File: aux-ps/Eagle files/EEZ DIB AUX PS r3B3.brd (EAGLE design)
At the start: 230.5 x 60 mm, 82 parts, among them IC1 BD00FC0WFP-E2, IC2 MAX31760AEE+, J1 PF0030/PC, J2 1-726388-2, J3 1-726388-2, J4 SWEB 8094 AU/GN, Q1 BTA26-600, Q2 BTA26-600, Q3 2N7002, Q4 2N7002, Q5 2N7002, SW1 DF62J12S2AHQA, SW2 EVQP7A01P, X1 39-28-1063, X2 39-30-1039, X3 DS1013-16SSIB1, X4 47053-1000, X5 N.C.

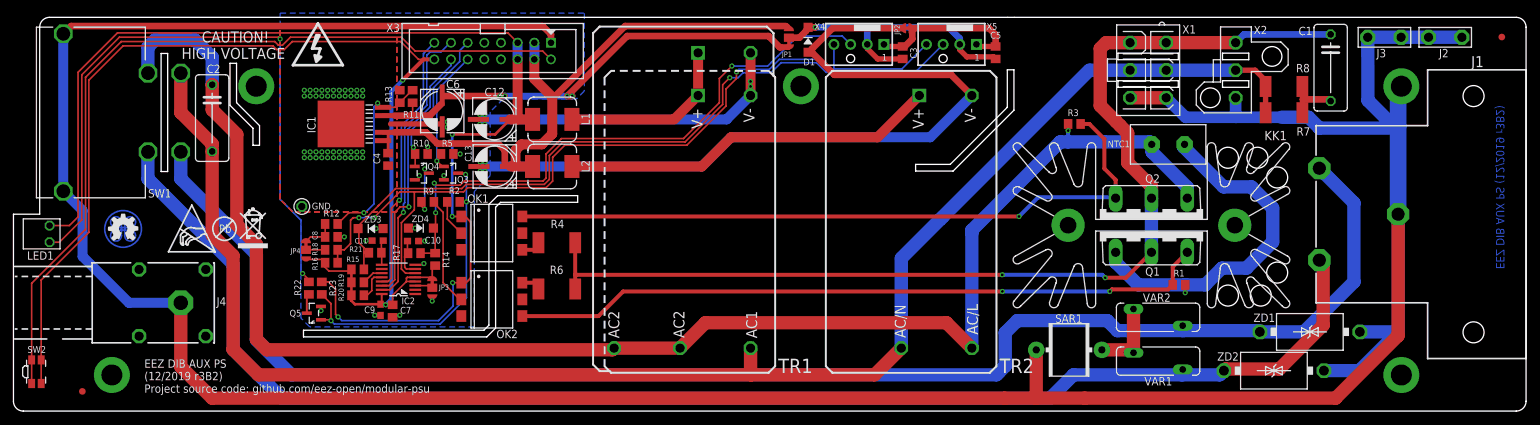
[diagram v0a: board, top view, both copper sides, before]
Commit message: #63, remove BOOT sw from AUX-PS
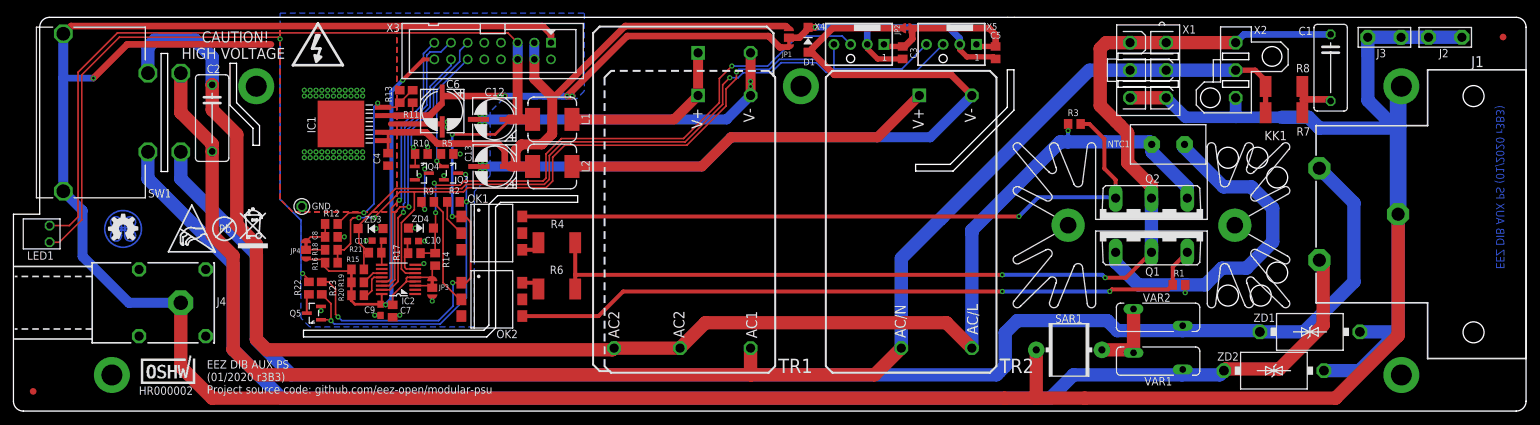
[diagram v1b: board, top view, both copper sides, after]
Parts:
- removed SW2: EVQP7A01P, EEZ_switches:PANASONIC_EVQP
- added OSHWA: HR000002, EEZ_Lib1:CERT-SMALL-SILK
- SW1: value DF62J12S2AHQA -> 1552.2602
- moved FM1 7.50 mm to (3.00, 3.00)
- moved FM2 0.20 mm to (227.0, 57.0)
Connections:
- net +3V3: no longer SW2.2.1, SW2.2.2
- net MBOOT: no longer SW2.1.1, SW2.1.2
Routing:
- net MBOOT: track 125.4 -> 0.00 mm
- net +3V3: track 182.6 -> 76.7 mm
- net PE: track 490.2 -> 524.0 mm, vias 2 -> 3
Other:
- board text added: "EEZ DIB AUX PS (01/2020 r3B3)"
- board text added: "EEZ DIB AUX PS (01/2020 r3B3) Project source code: github.com/eez-open/modular-psu"
- board text removed: "EEZ DIB AUX PS (12/2019 r3B2)"
- board text removed: "EEZ DIB AUX PS (12/2019 r3B2) Project source code: github.com/eez-open/modular-psu"

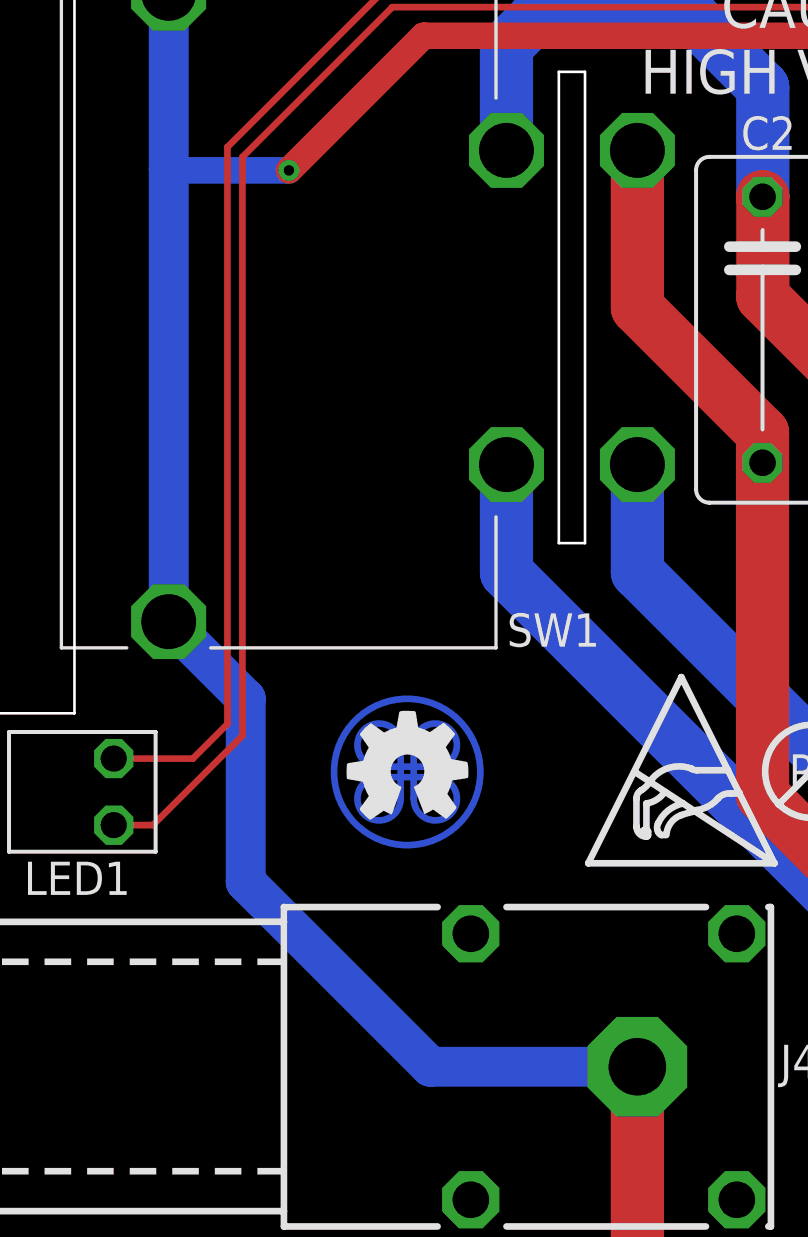
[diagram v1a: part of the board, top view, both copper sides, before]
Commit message: AUX-PS PCB layout update
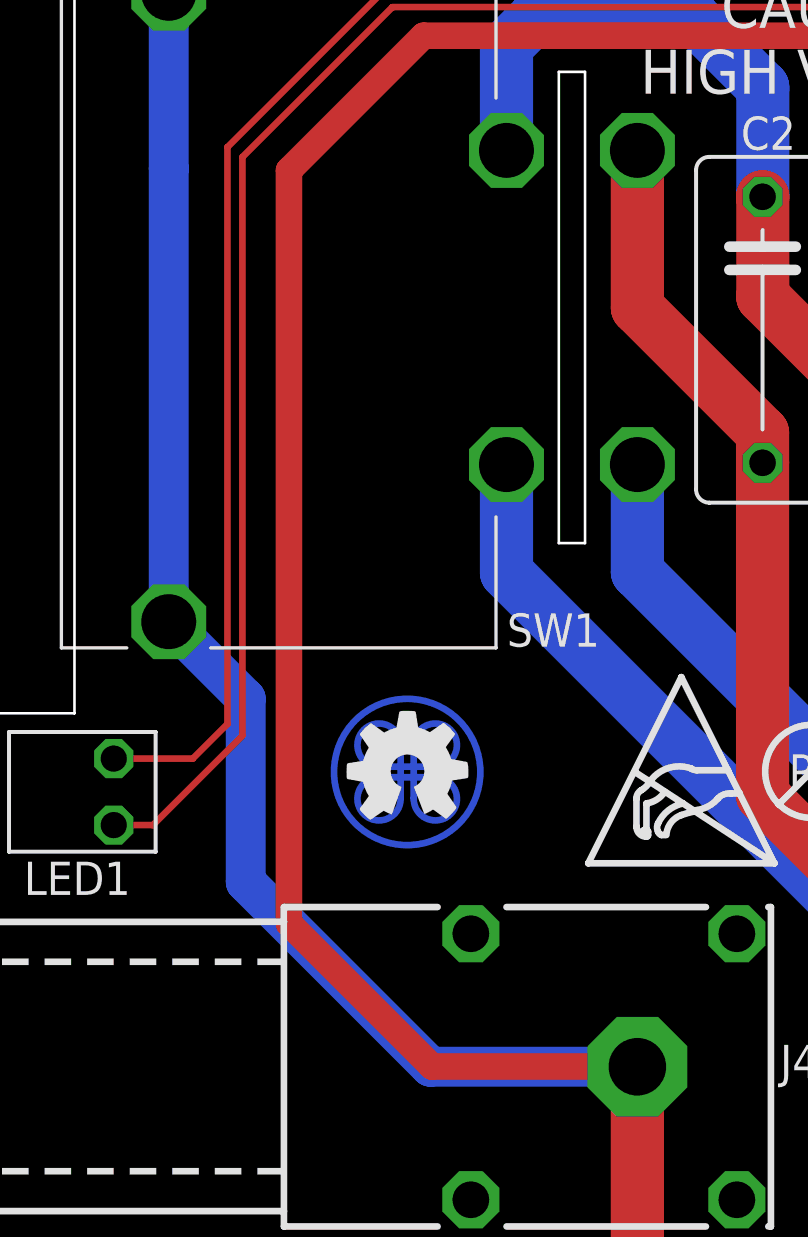
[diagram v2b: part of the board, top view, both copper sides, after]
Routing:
- net PE: track 524.0 -> 563.9 mm, vias 3 -> 2
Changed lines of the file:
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@@
 <grid distance="2.5" unitdist="mil" unit="mil" style="lines" multiple="40" display="no" altdistance="12.5" altunitdist="mil" altunit="mil"/>
 <layers>
-<layer number="1" name="Top" color="11" fill="1" visible="no" active="yes"/>
+<layer number="1" name="Top" color="11" fill="1" visible="yes" active="yes"/>
 <layer number="2" name="Route2" color="1" fill="3" visible="no" active="no"/>
 <layer number="3" name="Route3" color="4" fill="3" visible="no" active="no"/>
@@
 <layer number="14" name="Route14" color="1" fill="6" visible="no" active="no"/>
 <layer number="15" name="Route15" color="4" fill="6" visible="no" active="no"/>
-<layer number="16" name="Bottom" color="1" fill="1" visible="no" active="yes"/>
-<layer number="17" name="Pads" color="6" fill="1" visible="no" active="yes"/>
-<layer number="18" name="Vias" color="6" fill="1" visible="no" active="yes"/>
-<layer number="19" name="Unrouted" color="6" fill="1" visible="no" active="yes"/>
+<layer number="16" name="Bottom" color="1" fill="1" visible="yes" active="yes"/>
+<layer number="17" name="Pads" color="6" fill="1" visible="yes" active="yes"/>
+<layer number="18" name="Vias" color="6" fill="1" visible="yes" active="yes"/>
+<layer number="19" name="Unrouted" color="6" fill="1" visible="yes" active="yes"/>
 <layer number="20" name="Dimension" color="12" fill="1" visible="yes" active="yes"/>
 <layer number="21" name="tPlace" color="7" fill="1" visible="yes" active="yes"/>
@@
 <layer number="25" name="tNames" color="7" fill="1" visible="yes" active="yes"/>
 <layer number="26" name="bNames" color="13" fill="1" visible="no" active="yes"/>
-<layer number="27" name="tValues" color="14" fill="1" visible="yes" active="yes"/>
+<layer number="27" name="tValues" color="14" fill="1" visible="no" active="yes"/>
 <layer number="28" name="bValues" color="11" fill="1" visible="no" active="yes"/>
 <layer number="29" name="tStop" color="15" fill="1" visible="yes" active="yes"/>
@@
 <wire x1="211.455" y1="56.9595" x2="206.375" y2="56.9595" width="2.032" layer="16"/>
 <wire x1="17.3355" y1="55.88" x2="39.243" y2="55.88" width="1.016" layer="1"/>
-<via x="12.192" y="50.7365" extent="1-16" drill="0.4" shape="octagon"/>
-<wire x1="12.192" y1="50.7365" x2="7.6635" y2="50.7365" width="1.016" layer="16"/>
 <wire x1="7.6635" y1="50.7365" x2="7.6" y2="50.8" width="1.016" layer="16"/>
-<wire x1="25.5" y1="16.5" x2="29.3" y2="21.58" width="0" layer="19" extent="16-16"/>
-<wire x1="19.14" y1="21.58" x2="17.5995" y2="16.5" width="0" layer="19" extent="16-16"/>
-<wire x1="19.14" y1="11.42" x2="17.5995" y2="16.5" width="0" layer="19" extent="16-16"/>
+<wire x1="12.192" y1="50.7365" x2="12.192" y2="21.971" width="1.016" layer="1"/>
+<wire x1="12.192" y1="21.971" x2="17.653" y2="16.51" width="1.016" layer="1"/>
+<wire x1="17.653" y1="16.51" x2="25.527" y2="16.51" width="1.016" layer="1"/>
+<wire x1="17.3355" y1="55.88" x2="12.192" y2="50.7365" width="1.016" layer="1"/>
+<wire x1="25.527" y1="16.51" x2="29.3" y2="21.58" width="0" layer="19" extent="1-1"/>
+<wire x1="25.5" y1="16.5" x2="25.527" y2="16.51" width="0" layer="19" extent="1-16"/>
+<wire x1="19.14" y1="21.58" x2="17.653" y2="16.51" width="0" layer="19" extent="1-1"/>
+<wire x1="19.14" y1="11.42" x2="17.653" y2="16.51" width="0" layer="19" extent="1-1"/>
 <wire x1="29.3" y1="11.42" x2="25.5" y2="6.758" width="0" layer="19" extent="1-1"/>
 <wire x1="15" y1="5.5" x2="19.14" y2="11.42" width="0" layer="19" extent="1-1"/>
-<wire x1="17.3355" y1="55.88" x2="12.192" y2="50.7365" width="1.016" layer="1"/>
 </signal>
 <signal name="HOLE_UR">
